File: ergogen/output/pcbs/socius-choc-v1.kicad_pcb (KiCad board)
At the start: 2 copper layers, 117.6 x 96.6 mm, 156 parts

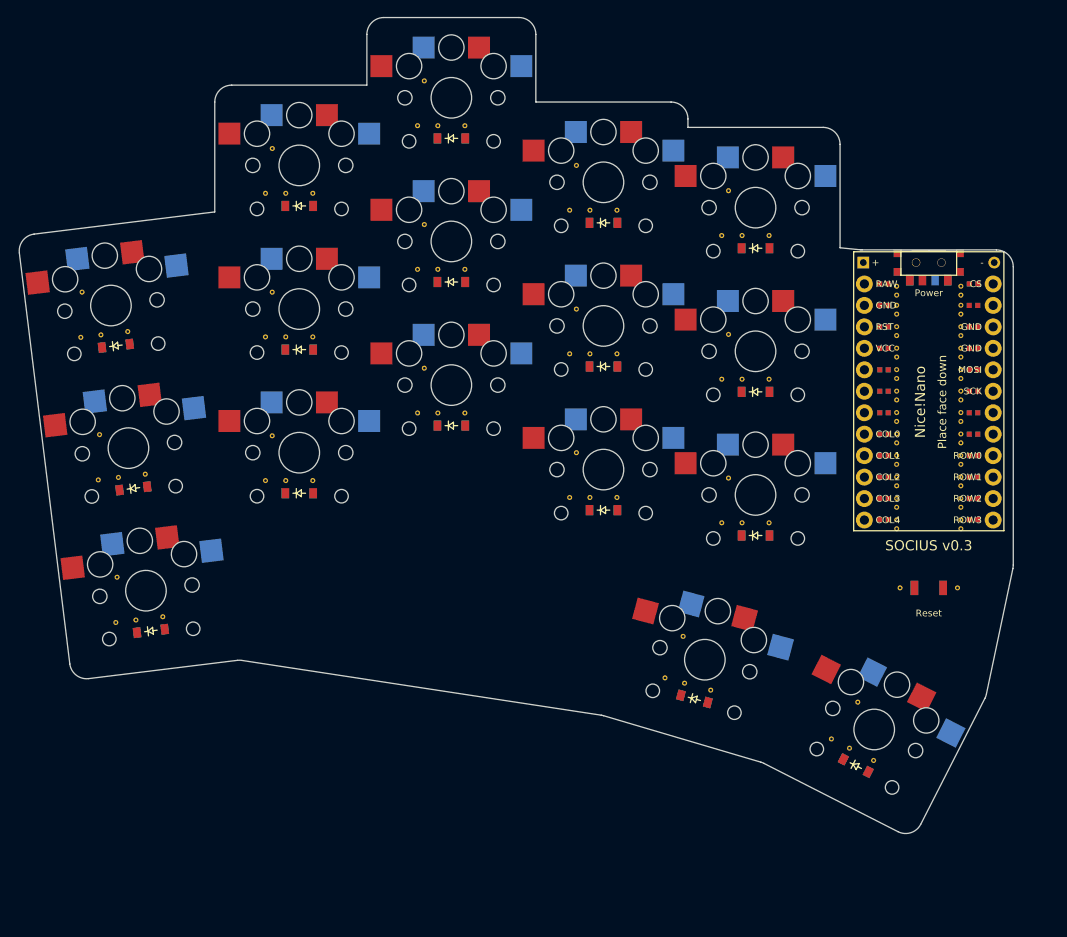
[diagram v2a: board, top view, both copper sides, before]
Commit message: adjusting dimensions after prototype 1
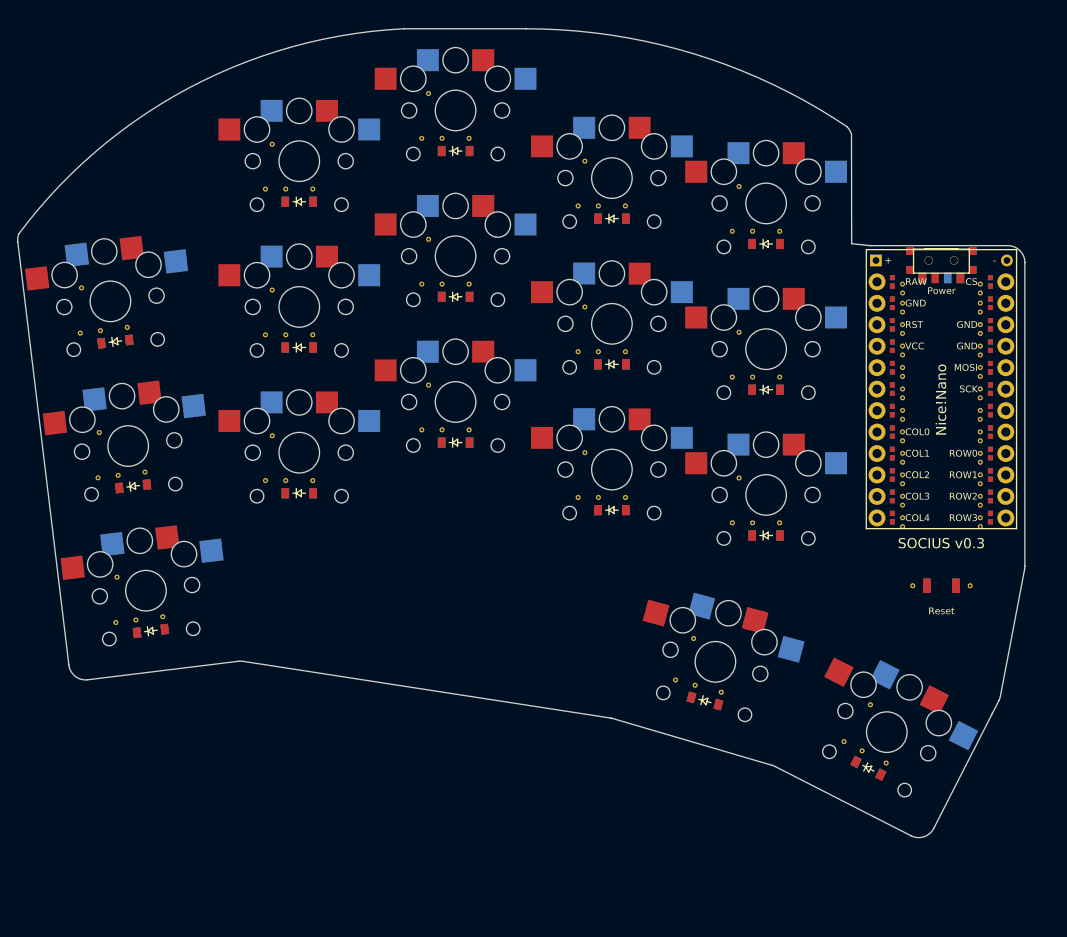
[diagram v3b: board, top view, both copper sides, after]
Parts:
- removed the REF** at (158.8, 163.5)
- removed the REF** at (212.5, 149.0)
- removed the REF** at (256.4, 142.5)
- removed the REF** at (248.8, 144.0)
- removed the REF** at (256.4, 144.0)
- removed the REF** at (248.8, 145.0)
- removed the REF** at (256.4, 145.0)
- removed the REF** at (248.8, 146.5)
- removed the REF** at (256.4, 146.5)
- removed the REF** at (248.8, 147.6)
- removed the REF** at (256.4, 147.6)
- removed the REF** at (248.8, 149.1)
- removed the REF** at (212.5, 132.0)
- removed the REF** at (256.4, 149.1)
- removed the REF** at (248.8, 150.1)
- removed the REF** at (256.4, 150.1)
- removed the REF** at (248.8, 151.6)
- removed the REF** at (256.4, 151.6)
- removed the REF** at (248.8, 152.7)
- removed the REF** at (256.4, 152.7)
- removed the REF** at (249.2, 159.7)
- removed the REF** at (256.0, 159.7)
- removed the REF** at (212.5, 115.0)
- removed the REF** at (230.5, 152.0)
- removed the REF** at (230.5, 135.0)
- removed the REF** at (230.5, 118.0)
- removed the REF** at (223.7, 170.9)
- removed the REF** at (243.3, 178.6)
- removed the REF** at (162.0, 163.1)
- removed the REF** at (159.9, 146.2)
- removed the REF** at (156.7, 146.6)
- removed the REF** at (157.8, 129.3)
- removed the REF** at (179.7, 147.0)
- removed the REF** at (179.7, 130.0)
- removed the REF** at (179.7, 113.0)
- removed the REF** at (197.7, 139.0)
- removed the REF** at (197.7, 122.0)
- removed the REF** at (197.7, 105.0)
- removed the REF** at (215.7, 149.0)
- removed the REF** at (215.7, 132.0)
- removed the REF** at (215.7, 115.0)
- removed the REF** at (154.7, 129.7)
- removed the REF** at (233.7, 152.0)
- removed the REF** at (233.7, 135.0)
- removed the REF** at (233.7, 118.0)
- removed the REF** at (226.8, 171.8)
- removed the REF** at (246.1, 180.1)
- removed the REF** at (156.4, 163.8)
- removed the REF** at (154.4, 146.9)
- removed the REF** at (152.3, 130.0)
- removed the REF** at (174.1, 147.0)
- removed the REF** at (174.1, 130.0)
- removed the REF** at (176.5, 147.0)
- removed the REF** at (174.1, 113.0)
- removed the REF** at (192.1, 139.0)
- removed the REF** at (192.1, 122.0)
- removed the REF** at (192.1, 105.0)
- removed the REF** at (210.1, 149.0)
- removed the REF** at (210.1, 132.0)
- removed the REF** at (210.1, 115.0)
- removed the REF** at (228.1, 152.0)
- removed the REF** at (228.1, 135.0)
- removed the REF** at (228.1, 118.0)
- removed the REF** at (176.5, 130.0)
- removed the REF** at (221.4, 170.3)
- removed the REF** at (241.1, 177.5)
- removed the REF** at (156.6, 158.4)
- removed the REF** at (154.5, 141.5)
- removed the REF** at (152.4, 124.7)
- removed the REF** at (174.9, 141.7)
- removed the REF** at (174.9, 124.7)
- removed the REF** at (174.9, 107.7)
- removed the REF** at (192.9, 133.7)
- removed the REF** at (192.9, 116.7)
- removed the REF** at (176.5, 113.0)
- removed the REF** at (192.9, 99.7)
- removed the REF** at (210.9, 143.7)
- removed the REF** at (210.9, 126.7)
- removed the REF** at (210.9, 109.7)
- removed the REF** at (228.9, 146.7)
- removed the REF** at (228.9, 129.7)
- removed the REF** at (228.9, 112.7)
- removed the REF** at (223.6, 165.4)
- removed the REF** at (244.2, 173.2)
- removed the REF** at (248.8, 124.0)
- removed the REF** at (194.5, 139.0)
- removed the REF** at (256.4, 124.0)
- removed the REF** at (248.8, 125.0)
- removed the REF** at (256.4, 125.0)
- removed the REF** at (248.8, 126.2)
- removed the REF** at (256.4, 126.2)
- removed the REF** at (248.8, 127.3)
- removed the REF** at (256.4, 127.3)
- removed the REF** at (248.8, 128.8)
- removed the REF** at (256.4, 128.8)
- removed the REF** at (248.8, 129.8)
- removed the REF** at (194.5, 122.0)
- removed the REF** at (256.4, 129.8)
- removed the REF** at (248.8, 131.3)
- removed the REF** at (256.4, 131.3)
- removed the REF** at (248.8, 132.3)
- removed the REF** at (256.4, 132.3)
- removed the REF** at (248.8, 133.8)
- removed the REF** at (256.4, 133.8)
- removed the REF** at (248.8, 134.9)
- removed the REF** at (256.4, 134.9)
- removed the REF** at (248.8, 136.4)
- removed the REF** at (194.5, 105.0)
- removed the REF** at (256.4, 136.4)
- removed the REF** at (248.8, 137.4)
- removed the REF** at (256.4, 137.4)
- removed the REF** at (248.8, 138.9)
- removed the REF** at (256.4, 138.9)
- removed the REF** at (248.8, 140.0)
- removed the REF** at (256.4, 140.0)
- removed the REF** at (248.8, 141.5)
- removed the REF** at (256.4, 141.5)
- removed the REF** at (248.8, 142.5)
- added REF**: VIA-0.6mm, VIA-0.6mm, F.Cu at (249.5, 151.4)
- added REF**: VIA-0.6mm, VIA-0.6mm, F.Cu at (213.5, 114.5)
- added REF**: VIA-0.6mm, VIA-0.6mm, F.Cu at (156.7, 146.3)
- added REF**: VIA-0.6mm, VIA-0.6mm, F.Cu at (230.2, 129.4)
- added REF**: VIA-0.6mm, VIA-0.6mm, F.Cu at (152.2, 129.5)
- added REF**: VIA-0.6mm, VIA-0.6mm, F.Cu at (174.1, 112.5)
- added REF**: VIA-0.6mm, VIA-0.6mm, F.Cu at (258.7, 143.7)
- added REF**: VIA-0.6mm, VIA-0.6mm, F.Cu at (249.5, 137.2)
- added REF**: VIA-0.6mm, VIA-0.6mm, F.Cu at (195.0, 106.5)
- added REF**: VIA-0.6mm, VIA-0.6mm, F.Cu at (154.6, 129.2)
- added REF**: VIA-0.6mm, VIA-0.6mm, F.Cu at (249.5, 149.9)
- added REF**: VIA-0.6mm, VIA-0.6mm, F.Cu at (258.7, 147.3)
- added REF**: VIA-0.6mm, VIA-0.6mm, F.Cu at (195.0, 141.0)
- added REF**: VIA-0.6mm, VIA-0.6mm, F.Cu at (216.7, 149.0)
- added REF**: VIA-0.6mm, VIA-0.6mm, F.Cu at (179.7, 147.0)
- added REF**: VIA-0.6mm, VIA-0.6mm, F.Cu at (258.7, 131.0)
- added REF**: VIA-0.6mm, VIA-0.6mm, F.Cu at (249.5, 132.1)
- added REF**: VIA-0.6mm, VIA-0.6mm, F.Cu at (249.5, 129.6)
- added REF**: VIA-0.6mm, VIA-0.6mm, F.Cu at (258.7, 124.8)
- added REF**: VIA-0.6mm, VIA-0.6mm, F.Cu at (193.4, 135.7)
- added REF**: VIA-0.6mm, VIA-0.6mm, F.Cu at (249.5, 128.5)
- added REF**: VIA-0.6mm, VIA-0.6mm, F.Cu at (192.6, 141.0)
- added REF**: VIA-0.6mm, VIA-0.6mm, F.Cu at (249.5, 143.7)
- added REF**: VIA-0.6mm, VIA-0.6mm, F.Cu at (231.8, 117.5)
- added REF**: VIA-0.6mm, VIA-0.6mm, F.Cu at (158.8, 163.5)
- added REF**: VIA-0.6mm, VIA-0.6mm, F.Cu at (249.5, 124.8)
- added REF**: VIA-0.6mm, VIA-0.6mm, F.Cu at (244.8, 179.0)
- added REF**: VIA-0.6mm, VIA-0.6mm, F.Cu at (192.6, 106.5)
- added REF**: VIA-0.6mm, VIA-0.6mm, F.Cu at (176.5, 112.5)
- added REF**: VIA-0.6mm, VIA-0.6mm, F.Cu at (249.5, 127.0)
- added REF**: VIA-0.6mm, VIA-0.6mm, F.Cu at (249.5, 133.6)
- added REF**: VIA-0.6mm, VIA-0.6mm, F.Cu at (249.5, 136.1)
- added REF**: VIA-0.6mm, VIA-0.6mm, F.Cu at (249.5, 142.3)
- added REF**: VIA-0.6mm, VIA-0.6mm, F.Cu at (179.7, 112.5)
- added REF**: VIA-0.6mm, VIA-0.6mm, F.Cu at (213.5, 149.0)
- added REF**: VIA-0.6mm, VIA-0.6mm, F.Cu at (258.7, 133.6)
- added REF**: VIA-0.6mm, VIA-0.6mm, F.Cu at (258.7, 146.3)
- added REF**: VIA-0.6mm, VIA-0.6mm, F.Cu at (176.5, 147.0)
- added REF**: VIA-0.6mm, VIA-0.6mm, F.Cu at (159.9, 146.0)
- added REF**: VIA-0.6mm, VIA-0.6mm, F.Cu at (258.7, 128.5)
- added REF**: VIA-0.6mm, VIA-0.6mm, F.Cu at (198.2, 123.7)
- added REF**: VIA-0.6mm, VIA-0.6mm, F.Cu at (258.7, 144.8)
- added REF**: VIA-0.6mm, VIA-0.6mm, F.Cu at (249.5, 126.0)
- added REF**: VIA-0.6mm, VIA-0.6mm, F.Cu at (154.3, 146.6)
- added REF**: VIA-0.6mm, VIA-0.6mm, F.Cu at (230.2, 146.7)
- added REF**: VIA-0.6mm, VIA-0.6mm, F.Cu at (258.7, 132.1)
- added REF**: VIA-0.6mm, VIA-0.6mm, F.Cu at (258.7, 141.2)
- added REF**: VIA-0.6mm, VIA-0.6mm, F.Cu at (193.4, 118.4)
- added REF**: VIA-0.6mm, VIA-0.6mm, F.Cu at (225.0, 171.2)
- added REF**: VIA-0.6mm, VIA-0.6mm, F.Cu at (258.7, 138.7)
- added REF**: VIA-0.6mm, VIA-0.6mm, F.Cu at (258.7, 137.2)
- added REF**: VIA-0.6mm, VIA-0.6mm, F.Cu at (249.5, 131.0)
- added REF**: VIA-0.6mm, VIA-0.6mm, F.Cu at (235.0, 134.7)
- added REF**: VIA-0.6mm, VIA-0.6mm, F.Cu at (249.5, 152.4)
- added REF**: VIA-0.6mm, VIA-0.6mm, F.Cu at (211.9, 143.7)
- added REF**: VIA-0.6mm, VIA-0.6mm, F.Cu at (258.7, 142.3)
- added REF**: VIA-0.6mm, VIA-0.6mm, F.Cu at (245.7, 173.5)
- added REF**: VIA-0.6mm, VIA-0.6mm, F.Cu at (174.9, 107.2)
- added REF**: VIA-0.6mm, VIA-0.6mm, F.Cu at (258.7, 129.6)
- added REF**: VIA-0.6mm, VIA-0.6mm, F.Cu at (249.5, 141.2)
- added REF**: VIA-0.6mm, VIA-0.6mm, F.Cu at (198.2, 141.0)
- added REF**: VIA-0.6mm, VIA-0.6mm, F.Cu at (258.7, 134.6)
- added REF**: VIA-0.6mm, VIA-0.6mm, F.Cu at (229.4, 134.7)
- added REF**: VIA-0.6mm, VIA-0.6mm, F.Cu at (249.5, 139.7)
- added REF**: VIA-0.6mm, VIA-0.6mm, F.Cu at (229.4, 117.5)
- added REF**: VIA-0.6mm, VIA-0.6mm, F.Cu at (198.2, 106.5)
- added REF**: VIA-0.6mm, VIA-0.6mm, F.Cu at (258.7, 148.8)
- added REF**: VIA-0.6mm, VIA-0.6mm, F.Cu at (211.1, 149.0)
- added REF**: VIA-0.6mm, VIA-0.6mm, F.Cu at (249.5, 138.7)
- added REF**: VIA-0.6mm, VIA-0.6mm, F.Cu at (231.8, 134.7)
- added REF**: VIA-0.6mm, VIA-0.6mm, F.Cu at (156.4, 163.8)
- added REF**: VIA-0.6mm, VIA-0.6mm, F.Cu at (249.5, 146.3)
- added REF**: VIA-0.6mm, VIA-0.6mm, F.Cu at (242.6, 177.9)
- added REF**: VIA-0.6mm, VIA-0.6mm, F.Cu at (162.0, 163.1)
- added REF**: VIA-0.6mm, VIA-0.6mm, F.Cu at (224.8, 165.7)
- added REF**: VIA-0.6mm, VIA-0.6mm, F.Cu at (249.5, 144.8)
- added REF**: VIA-0.6mm, VIA-0.6mm, F.Cu at (229.4, 152.0)
- added REF**: VIA-0.6mm, VIA-0.6mm, F.Cu at (249.5, 148.8)
- added REF**: VIA-0.6mm, VIA-0.6mm, F.Cu at (157.8, 128.8)
- added REF**: VIA-0.6mm, VIA-0.6mm, F.Cu at (193.4, 101.2)
- added REF**: VIA-0.6mm, VIA-0.6mm, F.Cu at (257.5, 159.4)
- added REF**: VIA-0.6mm, VIA-0.6mm, F.Cu at (211.9, 109.2)
- added REF**: VIA-0.6mm, VIA-0.6mm, F.Cu at (258.7, 151.4)
- added REF**: VIA-0.6mm, VIA-0.6mm, F.Cu at (195.0, 123.7)
- added REF**: VIA-0.6mm, VIA-0.6mm, F.Cu at (192.6, 123.7)
- added REF**: VIA-0.6mm, VIA-0.6mm, F.Cu at (174.9, 141.7)
- added REF**: VIA-0.6mm, VIA-0.6mm, F.Cu at (247.6, 180.4)
- added REF**: VIA-0.6mm, VIA-0.6mm, F.Cu at (258.7, 149.9)
- added REF**: VIA-0.6mm, VIA-0.6mm, F.Cu at (222.7, 170.6)
- added REF**: VIA-0.6mm, VIA-0.6mm, F.Cu at (211.9, 126.4)
- added REF**: VIA-0.6mm, VIA-0.6mm, F.Cu at (258.7, 126.0)
- added REF**: VIA-0.6mm, VIA-0.6mm, F.Cu at (249.5, 123.7)
- added REF**: VIA-0.6mm, VIA-0.6mm, F.Cu at (258.7, 152.4)
- added REF**: VIA-0.6mm, VIA-0.6mm, F.Cu at (154.5, 141.3)
- added REF**: VIA-0.6mm, VIA-0.6mm, F.Cu at (174.1, 147.0)
- added REF**: VIA-0.6mm, VIA-0.6mm, F.Cu at (216.7, 131.7)
- added REF**: VIA-0.6mm, VIA-0.6mm, F.Cu at (174.9, 124.4)
- added REF**: VIA-0.6mm, VIA-0.6mm, F.Cu at (258.7, 139.7)
- added REF**: VIA-0.6mm, VIA-0.6mm, F.Cu at (249.5, 134.6)
- added REF**: VIA-0.6mm, VIA-0.6mm, F.Cu at (179.7, 129.7)
- added REF**: VIA-0.6mm, VIA-0.6mm, F.Cu at (174.1, 129.7)
- added REF**: VIA-0.6mm, VIA-0.6mm, F.Cu at (216.7, 114.5)
- added REF**: VIA-0.6mm, VIA-0.6mm, F.Cu at (258.7, 123.7)
- added REF**: VIA-0.6mm, VIA-0.6mm, F.Cu at (231.8, 152.0)
- added REF**: VIA-0.6mm, VIA-0.6mm, F.Cu at (228.1, 172.0)
- added REF**: VIA-0.6mm, VIA-0.6mm, F.Cu at (249.5, 147.3)
- added REF**: VIA-0.6mm, VIA-0.6mm, F.Cu at (235.0, 117.5)
- added REF**: VIA-0.6mm, VIA-0.6mm, F.Cu at (156.6, 158.4)
- added REF**: VIA-0.6mm, VIA-0.6mm, F.Cu at (152.4, 124.2)
- added REF**: VIA-0.6mm, VIA-0.6mm, F.Cu at (250.7, 159.4)
- added REF**: VIA-0.6mm, VIA-0.6mm, F.Cu at (213.5, 131.7)
- added REF**: VIA-0.6mm, VIA-0.6mm, F.Cu at (211.1, 131.7)
- added REF**: VIA-0.6mm, VIA-0.6mm, F.Cu at (230.2, 112.2)
- added REF**: VIA-0.6mm, VIA-0.6mm, F.Cu at (258.7, 127.0)
- added REF**: VIA-0.6mm, VIA-0.6mm, F.Cu at (235.0, 152.0)
- added REF**: VIA-0.6mm, VIA-0.6mm, F.Cu at (258.7, 136.1)
- added REF**: VIA-0.6mm, VIA-0.6mm, F.Cu at (176.5, 129.7)
- added REF**: VIA-0.6mm, VIA-0.6mm, F.Cu at (211.1, 114.5)
- moved D7 2.06 mm to (196.6, 142.5)
- moved S7 2.06 mm to (196.6, 137.7)
- moved D8 1.82 mm to (196.6, 125.2)
- moved S8 1.82 mm to (196.6, 120.4)
- moved D9 1.58 mm to (196.6, 108.0)
- moved S9 1.58 mm to (196.6, 103.2)
- moved S17 1.52 mm to (247.7, 176.7)
- moved D17 1.52 mm to (245.5, 181.0)
- moved ? 1.52 mm to (254.1, 120.9)
- moved ? 1.52 mm to (254.1, 159.4)
- moved MCU1 1.52 mm to (254.1, 137.4)
- moved T1 1.52 mm to (254.1, 120.9)
- moved D15 1.35 mm to (233.4, 119.0)
- moved S15 1.35 mm to (233.4, 114.2)
- moved D16 1.27 mm to (226.2, 173.1)
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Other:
- board size 117.6 x 96.6 mm -> 119.2 x 95.7 mm
- net class Default removed

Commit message: altering key placement
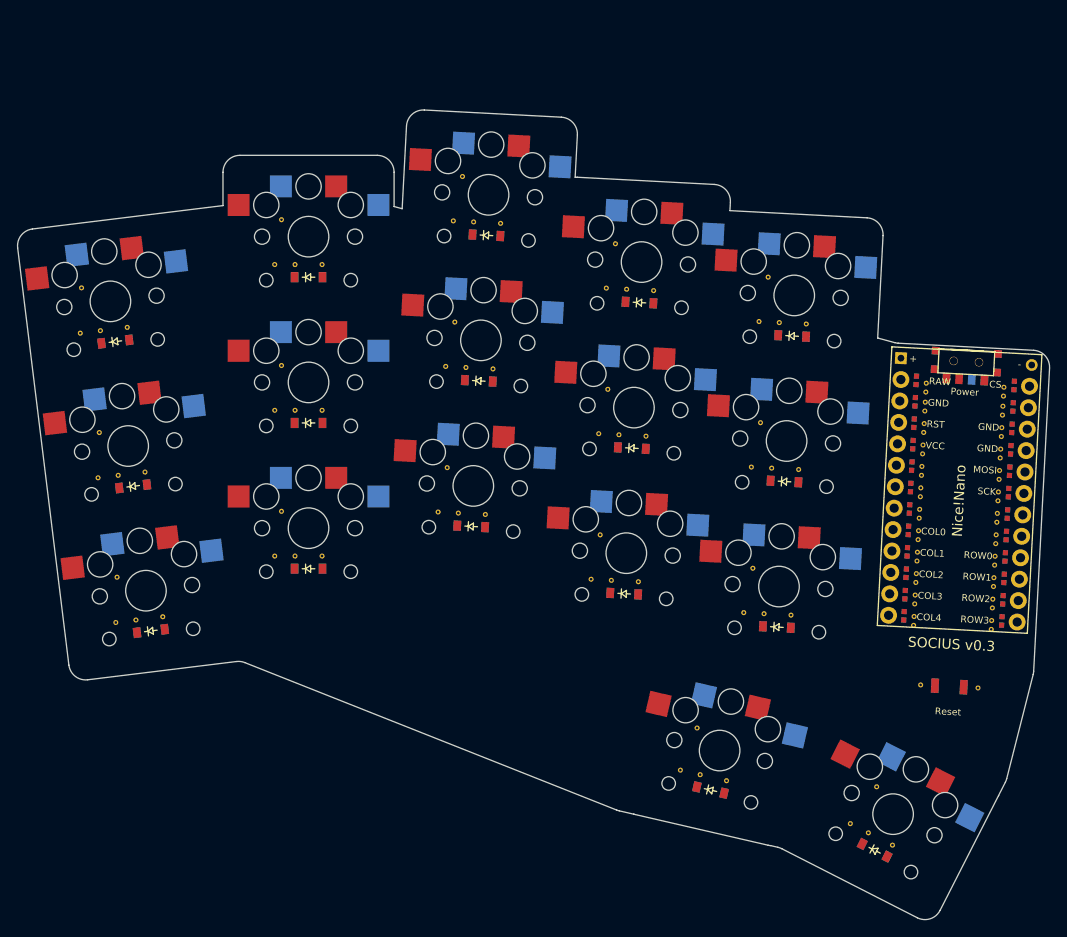
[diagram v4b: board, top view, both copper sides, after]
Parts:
- removed the REF** at (249.5, 151.4)
- removed the REF** at (213.5, 114.5)
- removed the REF** at (156.7, 146.3)
- removed the REF** at (230.2, 129.4)
- removed the REF** at (152.2, 129.5)
- removed the REF** at (174.1, 112.5)
- removed the REF** at (258.7, 143.7)
- removed the REF** at (249.5, 137.2)
- removed the REF** at (195.0, 106.5)
- removed the REF** at (154.6, 129.2)
- removed the REF** at (249.5, 149.9)
- removed the REF** at (258.7, 147.3)
- removed the REF** at (195.0, 141.0)
- removed the REF** at (216.7, 149.0)
- removed the REF** at (179.7, 147.0)
- removed the REF** at (258.7, 131.0)
- removed the REF** at (249.5, 132.1)
- removed the REF** at (249.5, 129.6)
- removed the REF** at (258.7, 124.8)
- removed the REF** at (193.4, 135.7)
- removed the REF** at (249.5, 128.5)
- removed the REF** at (192.6, 141.0)
- removed the REF** at (249.5, 143.7)
- removed the REF** at (231.8, 117.5)
- removed the REF** at (158.8, 163.5)
- removed the REF** at (249.5, 124.8)
- removed the REF** at (244.8, 179.0)
- removed the REF** at (192.6, 106.5)
- removed the REF** at (176.5, 112.5)
- removed the REF** at (249.5, 127.0)
- removed the REF** at (249.5, 133.6)
- removed the REF** at (249.5, 136.1)
- removed the REF** at (249.5, 142.3)
- removed the REF** at (179.7, 112.5)
- removed the REF** at (213.5, 149.0)
- removed the REF** at (258.7, 133.6)
- removed the REF** at (258.7, 146.3)
- removed the REF** at (176.5, 147.0)
- removed the REF** at (159.9, 146.0)
- removed the REF** at (258.7, 128.5)
- removed the REF** at (198.2, 123.7)
- removed the REF** at (258.7, 144.8)
- removed the REF** at (249.5, 126.0)
- removed the REF** at (154.3, 146.6)
- removed the REF** at (230.2, 146.7)
- removed the REF** at (258.7, 132.1)
- removed the REF** at (258.7, 141.2)
- removed the REF** at (193.4, 118.4)
- removed the REF** at (225.0, 171.2)
- removed the REF** at (258.7, 138.7)
- removed the REF** at (258.7, 137.2)
- removed the REF** at (249.5, 131.0)
- removed the REF** at (235.0, 134.7)
- removed the REF** at (249.5, 152.4)
- removed the REF** at (211.9, 143.7)
- removed the REF** at (258.7, 142.3)
- removed the REF** at (245.7, 173.5)
- removed the REF** at (174.9, 107.2)
- removed the REF** at (258.7, 129.6)
- removed the REF** at (249.5, 141.2)
- removed the REF** at (198.2, 141.0)
- removed the REF** at (258.7, 134.6)
- removed the REF** at (229.4, 134.7)
- removed the REF** at (249.5, 139.7)
- removed the REF** at (229.4, 117.5)
- removed the REF** at (198.2, 106.5)
- removed the REF** at (258.7, 148.8)
- removed the REF** at (211.1, 149.0)
- removed the REF** at (249.5, 138.7)
- removed the REF** at (231.8, 134.7)
- removed the REF** at (156.4, 163.8)
- removed the REF** at (249.5, 146.3)
- removed the REF** at (242.6, 177.9)
- removed the REF** at (162.0, 163.1)
- removed the REF** at (224.8, 165.7)
- removed the REF** at (249.5, 144.8)
- removed the REF** at (229.4, 152.0)
- removed the REF** at (249.5, 148.8)
- removed the REF** at (157.8, 128.8)
- removed the REF** at (193.4, 101.2)
- removed the REF** at (257.5, 159.4)
- removed the REF** at (211.9, 109.2)
- removed the REF** at (258.7, 151.4)
- removed the REF** at (195.0, 123.7)
- removed the REF** at (192.6, 123.7)
- removed the REF** at (174.9, 141.7)
- removed the REF** at (247.6, 180.4)
- removed the REF** at (258.7, 149.9)
- removed the REF** at (222.7, 170.6)
- removed the REF** at (211.9, 126.4)
- removed the REF** at (258.7, 126.0)
- removed the REF** at (249.5, 123.7)
- removed the REF** at (258.7, 152.4)
- removed the REF** at (154.5, 141.3)
- removed the REF** at (174.1, 147.0)
- removed the REF** at (216.7, 131.7)
- removed the REF** at (174.9, 124.4)
- removed the REF** at (258.7, 139.7)
- removed the REF** at (249.5, 134.6)
- removed the REF** at (179.7, 129.7)
- removed the REF** at (174.1, 129.7)
- removed the REF** at (216.7, 114.5)
- removed the REF** at (258.7, 123.7)
- removed the REF** at (231.8, 152.0)
- removed the REF** at (228.1, 172.0)
- removed the REF** at (249.5, 147.3)
- removed the REF** at (235.0, 117.5)
- removed the REF** at (156.6, 158.4)
- removed the REF** at (152.4, 124.2)
- removed the REF** at (250.7, 159.4)
- removed the REF** at (213.5, 131.7)
- removed the REF** at (211.1, 131.7)
- removed the REF** at (230.2, 112.2)
- removed the REF** at (258.7, 127.0)
- removed the REF** at (235.0, 152.0)
- removed the REF** at (258.7, 136.1)
- removed the REF** at (176.5, 129.7)
- removed the REF** at (211.1, 114.5)
- added REF**: VIA-0.6mm, VIA-0.6mm, F.Cu at (158.8, 163.5)
- added REF**: VIA-0.6mm, VIA-0.6mm, F.Cu at (215.1, 158.8)
- added REF**: VIA-0.6mm, VIA-0.6mm, F.Cu at (260.6, 154.4)
- added REF**: VIA-0.6mm, VIA-0.6mm, F.Cu at (251.3, 155.4)
- added REF**: VIA-0.6mm, VIA-0.6mm, F.Cu at (260.5, 155.9)
- added REF**: VIA-0.6mm, VIA-0.6mm, F.Cu at (251.2, 156.5)
- added REF**: VIA-0.6mm, VIA-0.6mm, F.Cu at (260.4, 157.0)
- added REF**: VIA-0.6mm, VIA-0.6mm, F.Cu at (251.2, 158.0)
- added REF**: VIA-0.6mm, VIA-0.6mm, F.Cu at (260.4, 158.5)
- added REF**: VIA-0.6mm, VIA-0.6mm, F.Cu at (251.1, 159.0)
- added REF**: VIA-0.6mm, VIA-0.6mm, F.Cu at (260.3, 159.5)
- added REF**: VIA-0.6mm, VIA-0.6mm, F.Cu at (251.0, 160.5)
- added REF**: VIA-0.6mm, VIA-0.6mm, F.Cu at (216.0, 141.5)
- added REF**: VIA-0.6mm, VIA-0.6mm, F.Cu at (260.2, 161.0)
- added REF**: VIA-0.6mm, VIA-0.6mm, F.Cu at (251.0, 161.6)
- added REF**: VIA-0.6mm, VIA-0.6mm, F.Cu at (260.2, 162.0)
- added REF**: VIA-0.6mm, VIA-0.6mm, F.Cu at (250.9, 163.1)
- added REF**: VIA-0.6mm, VIA-0.6mm, F.Cu at (260.1, 163.5)
- added REF**: VIA-0.6mm, VIA-0.6mm, F.Cu at (250.8, 164.1)
- added REF**: VIA-0.6mm, VIA-0.6mm, F.Cu at (260.0, 164.6)
- added REF**: VIA-0.6mm, VIA-0.6mm, F.Cu at (251.7, 171.2)
- added REF**: VIA-0.6mm, VIA-0.6mm, F.Cu at (258.5, 171.5)
- added REF**: VIA-0.6mm, VIA-0.6mm, F.Cu at (216.9, 124.3)
- added REF**: VIA-0.6mm, VIA-0.6mm, F.Cu at (233.1, 162.7)
- added REF**: VIA-0.6mm, VIA-0.6mm, F.Cu at (234.1, 145.5)
- added REF**: VIA-0.6mm, VIA-0.6mm, F.Cu at (235.0, 128.3)
- added REF**: VIA-0.6mm, VIA-0.6mm, F.Cu at (225.6, 181.8)
- added REF**: VIA-0.6mm, VIA-0.6mm, F.Cu at (245.5, 188.7)
- added REF**: VIA-0.6mm, VIA-0.6mm, F.Cu at (162.0, 163.1)
- added REF**: VIA-0.6mm, VIA-0.6mm, F.Cu at (159.9, 146.0)
- added REF**: VIA-0.6mm, VIA-0.6mm, F.Cu at (156.7, 146.3)
- added REF**: VIA-0.6mm, VIA-0.6mm, F.Cu at (157.8, 128.8)
- added REF**: VIA-0.6mm, VIA-0.6mm, F.Cu at (180.8, 155.9)
- added REF**: VIA-0.6mm, VIA-0.6mm, F.Cu at (180.8, 138.6)
- added REF**: VIA-0.6mm, VIA-0.6mm, F.Cu at (180.8, 121.4)
- added REF**: VIA-0.6mm, VIA-0.6mm, F.Cu at (200.2, 151.0)
- added REF**: VIA-0.6mm, VIA-0.6mm, F.Cu at (201.1, 133.8)
- added REF**: VIA-0.6mm, VIA-0.6mm, F.Cu at (202.0, 116.5)
- added REF**: VIA-0.6mm, VIA-0.6mm, F.Cu at (218.3, 158.9)
- added REF**: VIA-0.6mm, VIA-0.6mm, F.Cu at (219.2, 141.7)
- added REF**: VIA-0.6mm, VIA-0.6mm, F.Cu at (220.1, 124.5)
- added REF**: VIA-0.6mm, VIA-0.6mm, F.Cu at (154.6, 129.2)
- added REF**: VIA-0.6mm, VIA-0.6mm, F.Cu at (236.3, 162.9)
- added REF**: VIA-0.6mm, VIA-0.6mm, F.Cu at (237.2, 145.7)
- added REF**: VIA-0.6mm, VIA-0.6mm, F.Cu at (238.1, 128.4)
- added REF**: VIA-0.6mm, VIA-0.6mm, F.Cu at (228.7, 182.5)
- added REF**: VIA-0.6mm, VIA-0.6mm, F.Cu at (248.3, 190.1)
- added REF**: VIA-0.6mm, VIA-0.6mm, F.Cu at (156.4, 163.8)
- added REF**: VIA-0.6mm, VIA-0.6mm, F.Cu at (154.3, 146.6)
- added REF**: VIA-0.6mm, VIA-0.6mm, F.Cu at (152.2, 129.5)
- added REF**: VIA-0.6mm, VIA-0.6mm, F.Cu at (175.2, 155.9)
- added REF**: VIA-0.6mm, VIA-0.6mm, F.Cu at (175.2, 138.6)
- added REF**: VIA-0.6mm, VIA-0.6mm, F.Cu at (177.6, 155.9)
- added REF**: VIA-0.6mm, VIA-0.6mm, F.Cu at (175.2, 121.4)
- added REF**: VIA-0.6mm, VIA-0.6mm, F.Cu at (194.6, 150.7)
- added REF**: VIA-0.6mm, VIA-0.6mm, F.Cu at (195.5, 133.5)
- added REF**: VIA-0.6mm, VIA-0.6mm, F.Cu at (196.4, 116.2)
- added REF**: VIA-0.6mm, VIA-0.6mm, F.Cu at (212.7, 158.6)
- added REF**: VIA-0.6mm, VIA-0.6mm, F.Cu at (213.6, 141.4)
- added REF**: VIA-0.6mm, VIA-0.6mm, F.Cu at (214.5, 124.2)
- added REF**: VIA-0.6mm, VIA-0.6mm, F.Cu at (230.8, 162.6)
- added REF**: VIA-0.6mm, VIA-0.6mm, F.Cu at (231.7, 145.4)
- added REF**: VIA-0.6mm, VIA-0.6mm, F.Cu at (232.6, 128.1)
- added REF**: VIA-0.6mm, VIA-0.6mm, F.Cu at (177.6, 138.6)
- added REF**: VIA-0.6mm, VIA-0.6mm, F.Cu at (223.3, 181.2)
- added REF**: VIA-0.6mm, VIA-0.6mm, F.Cu at (243.4, 187.6)
- added REF**: VIA-0.6mm, VIA-0.6mm, F.Cu at (156.6, 158.4)
- added REF**: VIA-0.6mm, VIA-0.6mm, F.Cu at (154.5, 141.3)
- added REF**: VIA-0.6mm, VIA-0.6mm, F.Cu at (152.4, 124.2)
- added REF**: VIA-0.6mm, VIA-0.6mm, F.Cu at (176.0, 150.6)
- added REF**: VIA-0.6mm, VIA-0.6mm, F.Cu at (176.0, 133.3)
- added REF**: VIA-0.6mm, VIA-0.6mm, F.Cu at (176.0, 116.1)
- added REF**: VIA-0.6mm, VIA-0.6mm, F.Cu at (195.7, 145.4)
- added REF**: VIA-0.6mm, VIA-0.6mm, F.Cu at (196.6, 128.2)
- added REF**: VIA-0.6mm, VIA-0.6mm, F.Cu at (177.6, 121.4)
- added REF**: VIA-0.6mm, VIA-0.6mm, F.Cu at (197.5, 111.0)
- added REF**: VIA-0.6mm, VIA-0.6mm, F.Cu at (213.8, 153.4)
- added REF**: VIA-0.6mm, VIA-0.6mm, F.Cu at (214.7, 136.2)
- added REF**: VIA-0.6mm, VIA-0.6mm, F.Cu at (215.6, 118.9)
- added REF**: VIA-0.6mm, VIA-0.6mm, F.Cu at (231.8, 157.3)
- added REF**: VIA-0.6mm, VIA-0.6mm, F.Cu at (232.7, 140.1)
- added REF**: VIA-0.6mm, VIA-0.6mm, F.Cu at (233.6, 122.9)
- added REF**: VIA-0.6mm, VIA-0.6mm, F.Cu at (225.2, 176.2)
- added REF**: VIA-0.6mm, VIA-0.6mm, F.Cu at (246.5, 183.2)
- added REF**: VIA-0.6mm, VIA-0.6mm, F.Cu at (252.4, 135.4)
- added REF**: VIA-0.6mm, VIA-0.6mm, F.Cu at (197.0, 150.8)
- added REF**: VIA-0.6mm, VIA-0.6mm, F.Cu at (261.5, 135.9)
- added REF**: VIA-0.6mm, VIA-0.6mm, F.Cu at (252.3, 136.5)
- added REF**: VIA-0.6mm, VIA-0.6mm, F.Cu at (261.5, 137.0)
- added REF**: VIA-0.6mm, VIA-0.6mm, F.Cu at (252.2, 137.7)
- added REF**: VIA-0.6mm, VIA-0.6mm, F.Cu at (261.4, 138.2)
- added REF**: VIA-0.6mm, VIA-0.6mm, F.Cu at (252.2, 138.7)
- added REF**: VIA-0.6mm, VIA-0.6mm, F.Cu at (261.4, 139.2)
- added REF**: VIA-0.6mm, VIA-0.6mm, F.Cu at (252.1, 140.2)
- added REF**: VIA-0.6mm, VIA-0.6mm, F.Cu at (261.3, 140.7)
- added REF**: VIA-0.6mm, VIA-0.6mm, F.Cu at (252.0, 141.3)
- added REF**: VIA-0.6mm, VIA-0.6mm, F.Cu at (197.9, 133.6)
- added REF**: VIA-0.6mm, VIA-0.6mm, F.Cu at (261.2, 141.8)
- added REF**: VIA-0.6mm, VIA-0.6mm, F.Cu at (252.0, 142.8)
- added REF**: VIA-0.6mm, VIA-0.6mm, F.Cu at (261.2, 143.2)
- added REF**: VIA-0.6mm, VIA-0.6mm, F.Cu at (251.9, 143.8)
- added REF**: VIA-0.6mm, VIA-0.6mm, F.Cu at (261.1, 144.3)
- added REF**: VIA-0.6mm, VIA-0.6mm, F.Cu at (251.8, 145.3)
- added REF**: VIA-0.6mm, VIA-0.6mm, F.Cu at (261.0, 145.8)
- added REF**: VIA-0.6mm, VIA-0.6mm, F.Cu at (251.8, 146.3)
- added REF**: VIA-0.6mm, VIA-0.6mm, F.Cu at (261.0, 146.8)
- added REF**: VIA-0.6mm, VIA-0.6mm, F.Cu at (251.7, 147.8)
- added REF**: VIA-0.6mm, VIA-0.6mm, F.Cu at (198.8, 116.4)
- added REF**: VIA-0.6mm, VIA-0.6mm, F.Cu at (260.9, 148.3)
- added REF**: VIA-0.6mm, VIA-0.6mm, F.Cu at (251.6, 148.9)
- added REF**: VIA-0.6mm, VIA-0.6mm, F.Cu at (260.8, 149.4)
- added REF**: VIA-0.6mm, VIA-0.6mm, F.Cu at (251.6, 150.4)
- added REF**: VIA-0.6mm, VIA-0.6mm, F.Cu at (260.8, 150.8)
- added REF**: VIA-0.6mm, VIA-0.6mm, F.Cu at (251.5, 151.4)
- added REF**: VIA-0.6mm, VIA-0.6mm, F.Cu at (260.7, 151.9)
- added REF**: VIA-0.6mm, VIA-0.6mm, F.Cu at (251.4, 152.9)
- added REF**: VIA-0.6mm, VIA-0.6mm, F.Cu at (260.6, 153.4)
- added REF**: VIA-0.6mm, VIA-0.6mm, F.Cu at (251.4, 154.0)
- moved ? 12.3 mm to (257.1, 132.9), turned to -93 degrees
- moved T1 12.3 mm to (257.1, 132.9), turned to -3 degrees
- moved MCU1 12.1 mm to (256.2, 149.4), turned to -93 degrees
- moved ? 12.0 mm to (255.1, 171.3), turned to 177 degrees
- moved S15 11.4 mm to (236.7, 125.1), turned to -3 degrees
- moved D15 11.3 mm to (236.5, 129.9), turned to -3 degrees
- moved S14 11.1 mm to (235.8, 142.3), turned to -3 degrees
- moved D14 11.1 mm to (235.6, 147.1), turned to -3 degrees
- moved S13 10.9 mm to (234.9, 159.5), turned to -3 degrees
- moved D13 10.9 mm to (234.7, 164.3), turned to -3 degrees
- moved S9 10.7 mm to (200.5, 113.1), turned to -3 degrees
- moved D9 10.6 mm to (200.3, 117.9), turned to -3 degrees
- moved D16 10.6 mm to (226.8, 183.6), turned to -13 degrees
- moved S12 10.5 mm to (218.7, 121.1), turned to -3 degrees
- moved S16 10.5 mm to (227.9, 178.9), turned to -13 degrees
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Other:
- board size 119.2 x 95.7 mm -> 122.1 x 95.8 mm
- net class Default added: clearance 0.2, trace_width 0.25, via_dia 0.8, via_drill 0.4
